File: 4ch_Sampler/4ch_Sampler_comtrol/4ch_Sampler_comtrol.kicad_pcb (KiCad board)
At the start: 2 copper layers, 30 x 100 mm, 18 parts, among them J1 CH1, J2 CH2, J3 CH3, J4 CH4, J5 OUT, SW1 SW

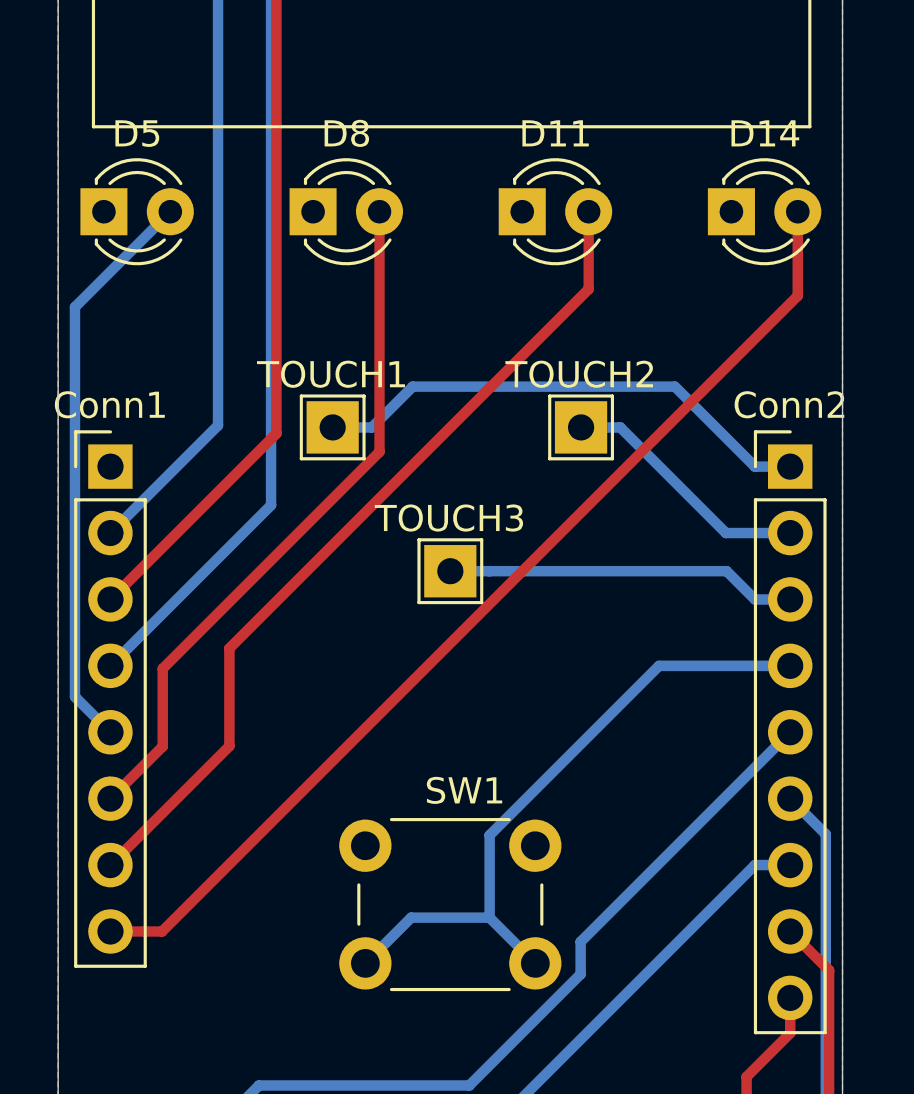
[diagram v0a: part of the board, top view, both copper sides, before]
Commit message: Ground plane fixed
Ground plane unconnected fixed and front pcb headers fliped to the back (footprint)
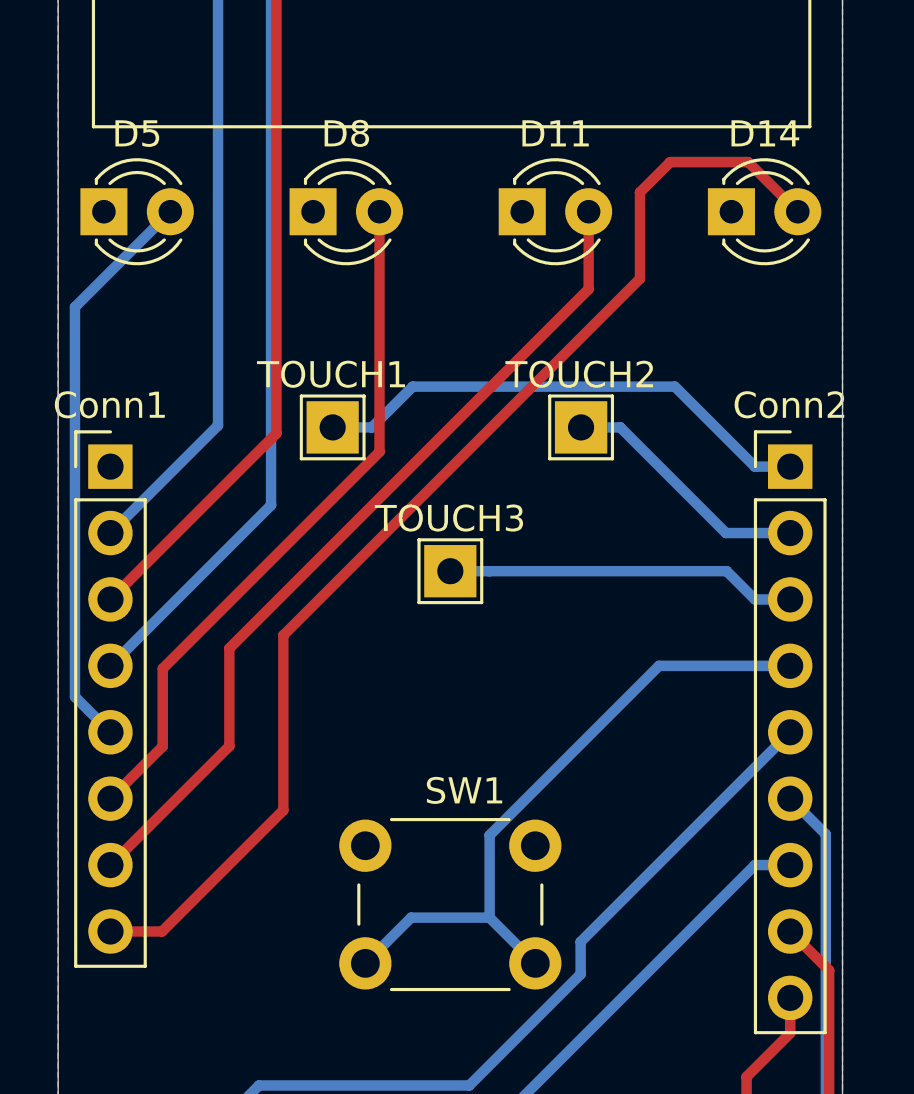
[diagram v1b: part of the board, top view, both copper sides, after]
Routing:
- net Net-(D12-Pad1): track 39.6 -> 45.1 mm

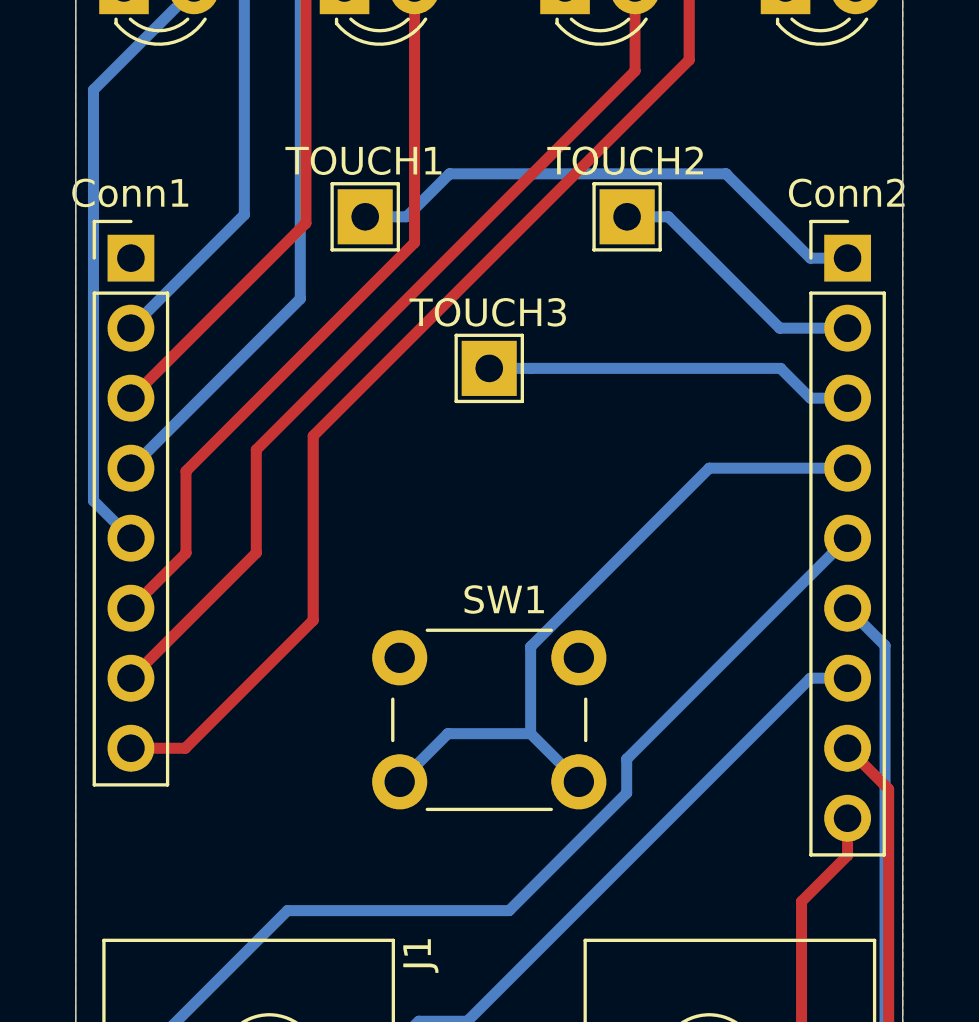
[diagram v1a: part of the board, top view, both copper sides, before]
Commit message: orientation headers and capacitors
Did a update on the headers. In 3d view some headers where pins changed to sockets. Did update previously on wrong board (flip header to wrong side) should be good now. Move bigger capacitors to the back of the board for more height possiblities.

Removed Gerber.zip added new gebers for this version in folders unzipped
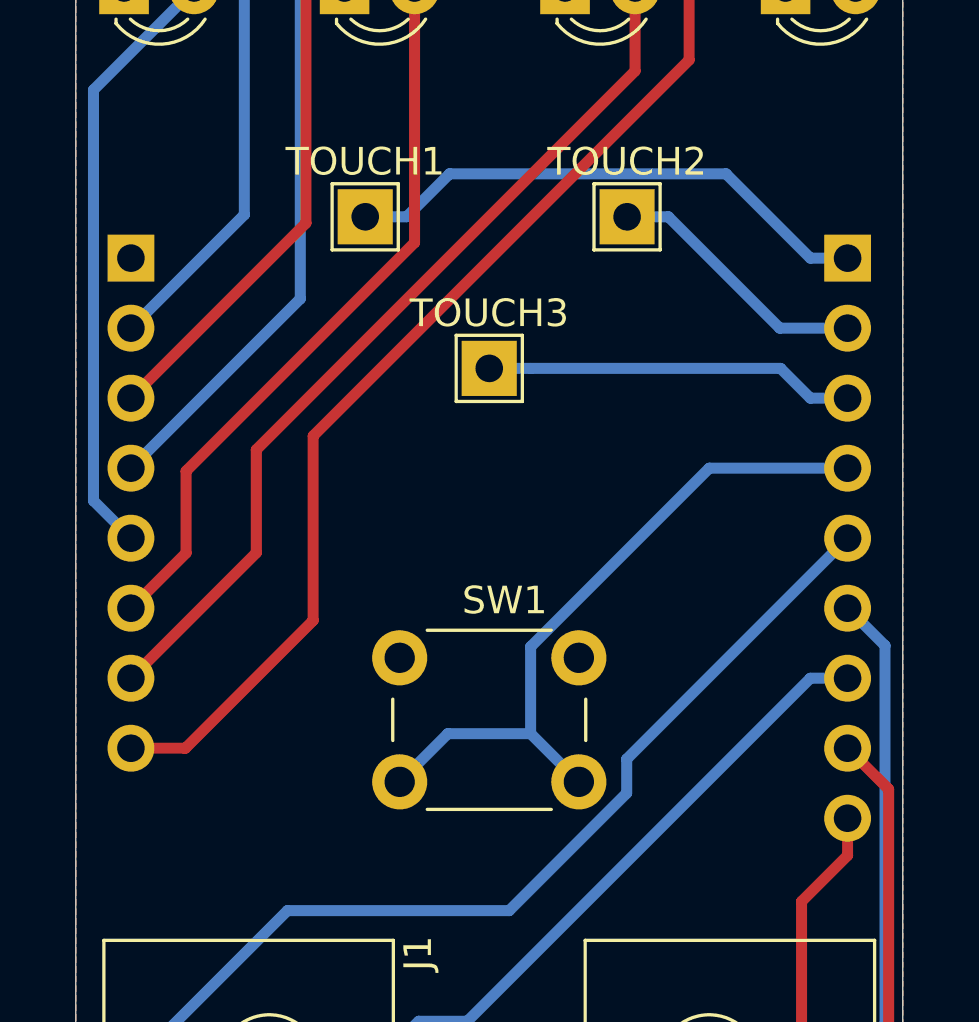
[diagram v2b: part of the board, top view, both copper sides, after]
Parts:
- Conn1, Conn2: moved to B.Cu
- turned Conn1 to 180 degrees
- turned Conn2 to 180 degrees
